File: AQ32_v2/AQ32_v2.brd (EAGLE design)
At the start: 57.1 x 57.1 mm, 115 parts, among them Q2 BCV27, Q3 BCV27, Q5 BCV27, Q6 BCV27, U1 ITG-3200, U10 MS5611, U11 MIC5239, U13 74AHC1G86DCK, U2 STM32F10XVXT6, U7 USD-SOCKETNEW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

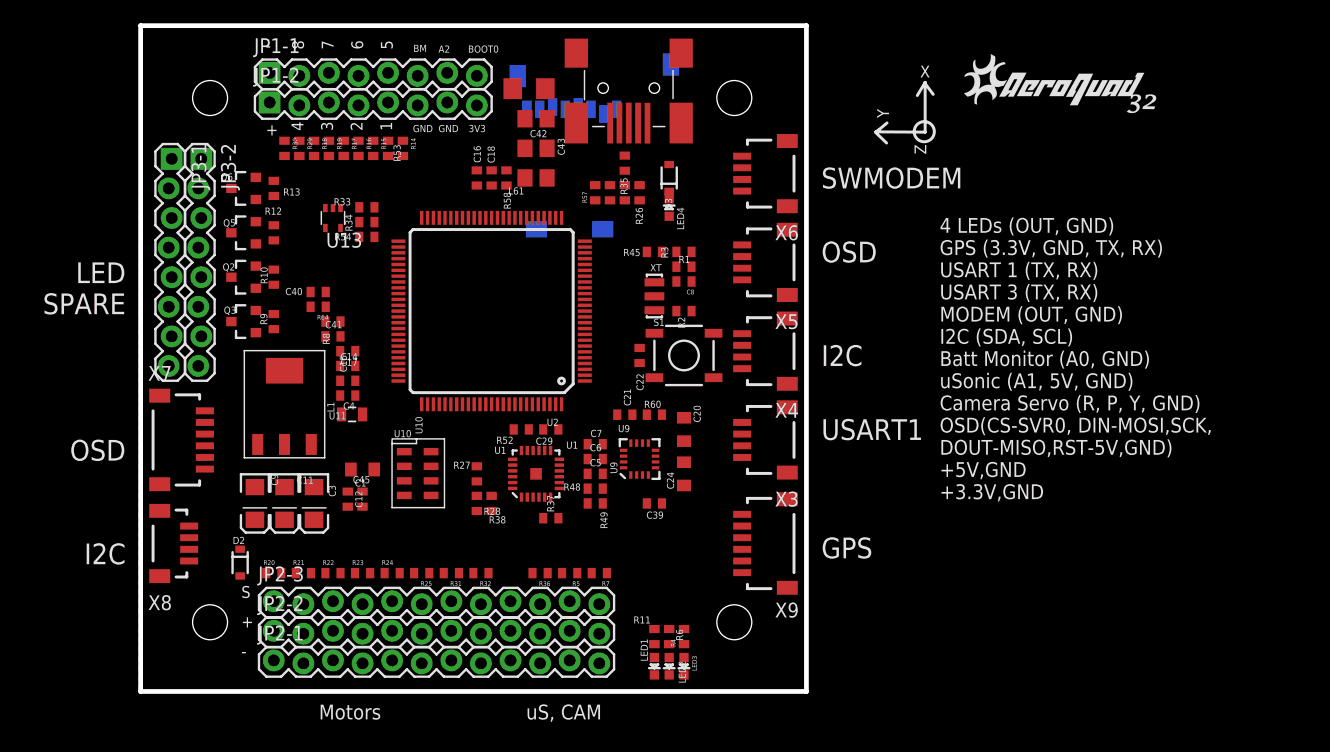
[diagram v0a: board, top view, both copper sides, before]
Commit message: completed connections to external JST connectors
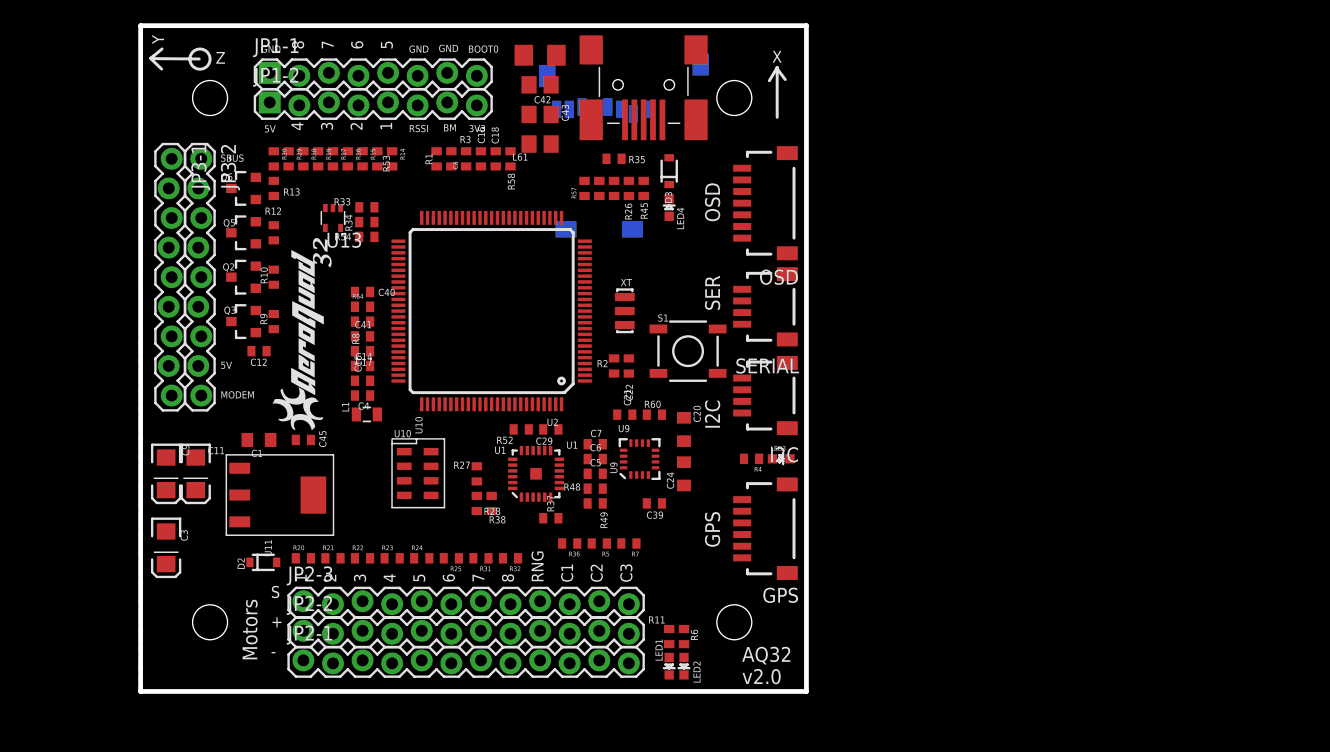
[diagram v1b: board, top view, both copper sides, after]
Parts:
- removed X3, X4, X5, X6: SM04B-SRSS-TB, con-jst2:SM04B-SRSS-TB
- removed X7, X9: SM06B-SRSS-TB, con-jst2:SM06B-SRSS-TB
- removed X8: BM04B-SRSS-TB, con-jst2:BM04B-SRSS-TB
- added GPS: SM06B-SRSS-TB, con-jst2:SM06B-SRSS-TB
- added I2C, SERIAL: SM04B-SRSS-TB, con-jst2:SM04B-SRSS-TB
- added OSD: SM07B-SRSS-TB, con-jst2:SM07B-SRSS-TB
- JP3-1, JP3-2: value (none) -> M09LOCK; device SparkFun-Connectors:1X08_LOCK -> SparkFun-Connectors:1X09_LOCK
- moved U$4 60.3 mm to (16.7, 22.4), turned to 90 degrees
- moved R1 22.7 mm to (25.4, 45.7), turned to 90 degrees
- moved R3 22.0 mm to (26.7, 45.7), turned to 270 degrees
- moved C8 21.5 mm to (27.9, 45.7), turned to 90 degrees
- moved LED3 19.7 mm to (55.0, 20.0), turned to 270 degrees
- moved R4 16.3 mm to (52.4, 20.0), turned to 180 degrees
- moved C12 14.8 mm to (10.2, 29.2), turned to 180 degrees
- moved C3 13.3 mm to (2.19, 12.3)
- moved U$5 11.8 mm to (18.4, 38.5), turned to 0 degrees
- moved C1 9.25 mm to (10.2, 21.6)
- moved C11 8.03 mm to (4.73, 18.7)
- moved C9 8.03 mm to (2.19, 18.7)
- moved R2 7.63 mm to (40.6, 27.9), turned to 90 degrees
- moved C45 7.18 mm to (14.0, 21.6), turned to 0 degrees
- moved U11 5.80 mm to (8.52, 16.9), turned to 270 degrees
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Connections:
- net OUT3 renamed LEDGND3
- removed net N$16: JP1-1.6
- removed net N$17: JP1-1.7
- removed net N$4: JP2-3.9
- removed net OUT1: JP3-2.1, Q5.3
- removed net OUT2: JP3-2.2, Q2.3
- removed net OUT4: JP3-2.4, Q6.3
- new net LEDGND1: JP3-2.2, Q5.3
- new net LEDGND2: JP3-1.2, Q2.3
- new net LEDGND4: JP3-1.3, Q6.3
- new net NSS_LV/DAC_OUT1: JP3-2.9
- net 3V3AN: now also I2C.1, JP3-2.7, SERIAL.1
- net 3V3DIG: now also GPS.4; no longer X9.4
- net 5V-3: now also OSD.1, OSD.6
- net 5V-4: now also JP3-2.8
- net ADC123_IN12: now also JP3-1.4
- net ADC123_IN13: now also JP1-2.6
- net ADC12_IN14: now also JP3-1.7
- net ADC12_IN15: now also JP3-1.5
- net GND: now also GPS.3, I2C.4, JP1-1.6, JP1-1.7, JP3-1.8, JP3-1.9, OSD.7, SERIAL.4; no longer JP1-2.7, JP3-1.1, JP3-1.2, JP3-1.3, JP3-1.4, X9.3
- net GPSBATT: now also GPS.5; no longer X9.5
- net GPSLED: now also GPS.6; no longer X9.6
- net JTAG-TRST: now also JP3-2.6
- net JTCK: now also JP3-2.5
- net JTMS: now also JP3-2.4
- net LIPO: now also JP1-2.7; no longer JP1-2.6
- net MISO2_LV: now also OSD.5
- net MOSI2_LV: now also OSD.3
- net SCK2_LV: now also OSD.4
- net SCL2_LV: now also I2C.2
- net SDA2_LV: now also I2C.3
- net TIM3_CH3: now also JP2-3.9
- net TIM3_CH4: now also JP3-1.6
- net TIM5_CH4: now also OSD.2
- net UART1_RX: now also SERIAL.3
- net UART1_TX: now also SERIAL.2
- net UART2_RX: now also GPS.2; no longer X9.2
- net UART2_TX: now also GPS.1; no longer X9.1
- net UART3_RX: now also JP3-2.1
- net UART3_TX: now also JP3-1.1
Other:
- board text added: "5V"
- board text added: "AQ32 v2.0"
- board text added: "C1"
- board text added: "C2"
- board text added: "C3"
- board text added: "MODEM"
- board text added: "RNG"
- board text added: "RSSI"
- board text added: "SBUS"
- board text added: "SER"
- board text removed: "4 LEDs (OUT, GND) GPS (3.3V, GND, TX, RX) USART 1 (TX, RX) USART 3 (TX, RX) MODEM (OUT, GND) I2C (SDA, SCL) Batt Monitor (A0, GND) uSonic (A1, 5V, GND) Camera Servo (R, P, Y, GND) OSD(CS-SVR0, DIN-MOSI,SCK, DOUT-MISO,RST-5V,GND) +5V,GND +3.3V,GND"
- board text removed: "A2"
- board text removed: "LED SPARE"
- board text removed: "SWMODEM"
- board text removed: "USART1"
- board text removed: "uS, CAM"

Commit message: move LEDs to separate connector, connected baro to SPI
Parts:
- removed L61: (no value), rcl:R0805
- added JP4-1, JP4-2: (no value), SparkFun-Connectors:1X02_LOCK
- added JP5: M01PTH, SparkFun-Connectors:1X01
- added L2: 22uH, SparkFun:0805
- added R39: 10K, SparkFun:C0402
- C1: value 10uF -> 4.7uF
- D2, D3: value (none) -> 30V
- JP3-1, JP3-2: value M09LOCK -> M09; device SparkFun-Connectors:1X09_LOCK -> SparkFun-Connectors:1X09
- R11, R4, R57, R6: value 294R -> 330
- moved R52 30.0 mm to (31.4, 52.4), turned to 90 degrees
- moved C39 28.1 mm to (16.5, 21.6), turned to 270 degrees
- moved C15 25.7 mm to (43.2, 35.6), turned to 0 degrees
- moved U9 18.2 mm to (43.2, 38.1)
- moved C21 17.0 mm to (43.2, 40.6)
- moved C24 16.9 mm to (47.0, 35.6)
- moved C20 16.9 mm to (47.0, 39.4)
- moved R58 16.3 mm to (41.9, 33.0), turned to 180 degrees
- moved C40 12.8 mm to (17.8, 21.6), turned to 270 degrees
- moved C1 12.7 mm to (22.9, 21.6)
- moved R45 11.5 mm to (41.9, 31.8), turned to 180 degrees
- moved C14 10.9 mm to (10.2, 21.6), turned to 270 degrees
- moved R48 9.00 mm to (47.0, 21.6)
- moved R49 9.00 mm to (47.0, 20.3)
- moved C9 8.99 mm to (7.97, 11.8), turned to 90 degrees
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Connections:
- removed net NSS_LV/DAC_OUT1: JP3-2.9
- removed net PD10: U2.57
- removed net PE7: U2.38
- new net BARO_CS: R39.1, U10.4, U10.5, U2.57
- new net BARO_PS: U10.2, U2.38
- net 3V3AN: no longer JP3-2.7
- net 3V3DIG: now also L2.1, R39.2; no longer L61.1, U10.2, U10.4, U10.5
- net 5V-2: now also JP2-2.10, JP2-2.11, JP2-2.12; no longer JP2-2.9
- net 5V-3: now also JP2-2.9; no longer JP2-2.10, JP2-2.11, JP2-2.12
- net 5V-4: no longer JP3-2.8
- net 5VIN: now also JP3-2.1
- net ADC123_IN12: now also JP3-2.8; no longer JP3-1.4
- net ADC12_IN14: now also JP3-2.5; no longer JP3-1.7
- net ADC12_IN15: now also JP3-2.7; no longer JP3-1.5
- net GND: now also JP3-1.1, JP3-1.4, JP3-1.5, JP3-1.6, JP3-1.7
- net GPSBATT: now also JP5.1
- net JTAG-TRST: now also JP3-1.3; no longer JP3-2.6
- net JTCK: now also JP3-2.4; no longer JP3-2.5
- net JTMS: now also JP3-2.3; no longer JP3-2.4
- net LEDGND1: now also JP4-1.1; no longer JP3-2.2
- net LEDGND2: now also JP4-1.2; no longer JP3-1.2
- net LEDGND3: now also JP4-2.1; no longer JP3-2.3
- net LEDGND4: now also JP4-2.2; no longer JP3-1.3
- net N$40: now also L2.2; no longer L61.2
- net NSS1_LV/DAC_OUT1: now also JP3-2.9
- net TIM3_CH4: now also JP3-2.6; no longer JP3-1.6
- net UART3_RX: now also JP3-2.2; no longer JP3-2.1
- net UART3_TX: now also JP3-1.2; no longer JP3-1.1
- net UART4_RX: now also U10.6
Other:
- board text added: "AI2"
- board text added: "AI3"
- board text added: "AI4"
- board text added: "AI5"
- board text added: "Camera"
- board text added: "JTCK"
- board text added: "JTMS"
- board text added: "LED GND"
- board text removed: "C1"
- board text removed: "C2"
- board text removed: "C3"

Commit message: added ground pin for GPS battery
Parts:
- JP5: value M01PTH -> (none); device SparkFun-Connectors:1X01 -> SparkFun-Connectors:1X02
- moved JP5 8.52 mm to (45.7, 11.4)
- moved R37 0.99 mm to (41.9, 14.0)
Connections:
- net GND: now also JP5.1
- net GPSBATT: now also JP5.2; no longer JP5.1
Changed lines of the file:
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@@
 <text x="6.8066" y="28.9334" size="0.6096" layer="21" font="vector">JTCK</text>
 <text x="6.8066" y="16.2334" size="0.6096" layer="21" font="vector">MODEM</text>
+<text x="47.9" y="8.88" size="1.016" layer="21">+</text>
+<text x="45.39" y="8.94" size="1.016" layer="21">-</text>
 </plain>
 <attributes>
@@
 <attribute name="VALUE" x="46.06" y="15.28" size="1.27" layer="27" rot="R90"/>
 </element>
-<element name="R37" library="resistor" package="R0402" value="0R" x="42.83" y="13.6" smashed="yes">
-<attribute name="NAME" x="43.124" y="14.117" size="0.6096" layer="25" rot="R90"/>
-<attribute name="VALUE" x="42.195" y="11.568" size="1.27" layer="27"/>
+<element name="R37" library="resistor" package="R0402" value="0R" x="41.91" y="13.97" smashed="yes">
+<attribute name="NAME" x="42.204" y="14.487" size="0.6096" layer="25" rot="R90"/>
+<attribute name="VALUE" x="41.275" y="11.938" size="1.27" layer="27"/>
 </element>
 <element name="R38" library="resistor" package="R0402" value="0R" x="38.1" y="15.24" smashed="yes" rot="R270">
@@
 <element name="JP3-2" library="SparkFun-Connectors" package="1X09" value="M09" x="5.08" y="38.1" rot="R270"/>
 <element name="R39" library="SparkFun" package="C0402" value="10K" x="21.59" y="15.24" rot="R90"/>
-<element name="JP5" library="SparkFun-Connectors" package="1X01" value="M01PTH" x="49.53" y="19.05"/>
+<element name="JP5" library="SparkFun-Connectors" package="1X02" value="" x="45.72" y="11.43"/>
 </elements>
 <signals>
@@
 <wire x1="26.2" y1="18.04" x2="31.75" y2="19.7" width="0" layer="19" extent="1-1"/>
 <wire x1="43.91" y1="16.53" x2="33.4" y2="22.11" width="0" layer="19" extent="1-1"/>
-<wire x1="43.48" y1="13.6" x2="43.91" y2="16.53" width="0" layer="19" extent="1-1"/>
+<wire x1="42.56" y1="13.97" x2="43.91" y2="16.53" width="0" layer="19" extent="1-1"/>
 </signal>
 <signal name="N$1">
@@
 <contactref element="U1" pad="23"/>
 <contactref element="R37" pad="1"/>
-<wire x1="42.18" y1="13.6" x2="39.91" y2="17.03" width="0" layer="19" extent="1-1"/>
+<wire x1="41.26" y1="13.97" x2="39.91" y2="17.03" width="0" layer="19" extent="1-1"/>
 <wire x1="26.4" y1="22.11" x2="39.91" y2="17.03" width="0" layer="19" extent="1-1"/>
 </signal>
@@
 <contactref element="JP3-1" pad="8"/>
 <contactref element="JP3-1" pad="9"/>
+<contactref element="JP5" pad="1"/>
 <wire x1="41.58" y1="49.07" x2="48.06" y2="53.82" width="0" layer="19" extent="1-16"/>
 <wire x1="37.9" y1="50.17" x2="41.58" y2="49.07" width="0" layer="19" extent="1-16"/>
@@
 <wire x1="47.64" y1="16.51" x2="43.91" y2="18.53" width="0" layer="19" extent="1-1"/>
 <wire x1="47.64" y1="15.24" x2="47.64" y2="16.51" width="0" layer="19" extent="1-1"/>
+<wire x1="45.72" y1="11.43" x2="47.64" y2="16.51" width="0" layer="19" extent="1-1"/>
 <wire x1="51.635" y1="13.47" x2="47.64" y2="15.24" width="0" layer="19" extent="1-1"/>
 <wire x1="36.9" y1="22.11" x2="40.66" y2="19.78" width="0" layer="19" extent="1-1"/>
 <wire x1="51.635" y1="34.52" x2="46.99" y2="34.56" width="0" layer="19" extent="1-1"/>
 <wire x1="51.635" y1="44.91" x2="46.47" y2="43.18" width="0" layer="19" extent="1-1"/>
+<wire x1="55.73" y1="19.97" x2="45.72" y2="11.43" width="0" layer="19" extent="1-1"/>
 <wire x1="51.635" y1="26.9" x2="44.45" y2="27.305" width="0" layer="19" extent="1-1"/>
-<wire x1="55.73" y1="19.97" x2="51.635" y2="13.47" width="0" layer="19" extent="1-1"/>
 <wire x1="12.43" y1="36.51" x2="21.17" y2="38.75" width="0" layer="19" extent="1-1"/>
 <wire x1="9.89" y1="39.05" x2="12.43" y2="36.51" width="0" layer="19" extent="1-1"/>
@@
 <signal name="GPSBATT">
 <contactref element="GPS" pad="5"/>
-<contactref element="JP5" pad="1"/>
-<wire x1="49.53" y1="19.05" x2="51.635" y2="15.47" width="0" layer="19" extent="1-1"/>
+<contactref element="JP5" pad="2"/>
+<wire x1="51.635" y1="15.47" x2="48.26" y2="11.43" width="0" layer="19" extent="1-1"/>
 </signal>
 <signal name="5V-1" class="1">
